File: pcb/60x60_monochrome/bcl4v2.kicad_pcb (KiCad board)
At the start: 2 copper layers, 60 x 60 mm, 56 parts, among them J1 Conn_01x05, J10 Conn_01x01_Female, J11 Conn_01x01_Female, J12 Conn_01x01_Female, J13 Conn_01x01_Female, J14 Conn_01x02, J15 Conn_01x04, J2 Conn_01x05, J3 USB_OTG, J4 Conn_01x05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

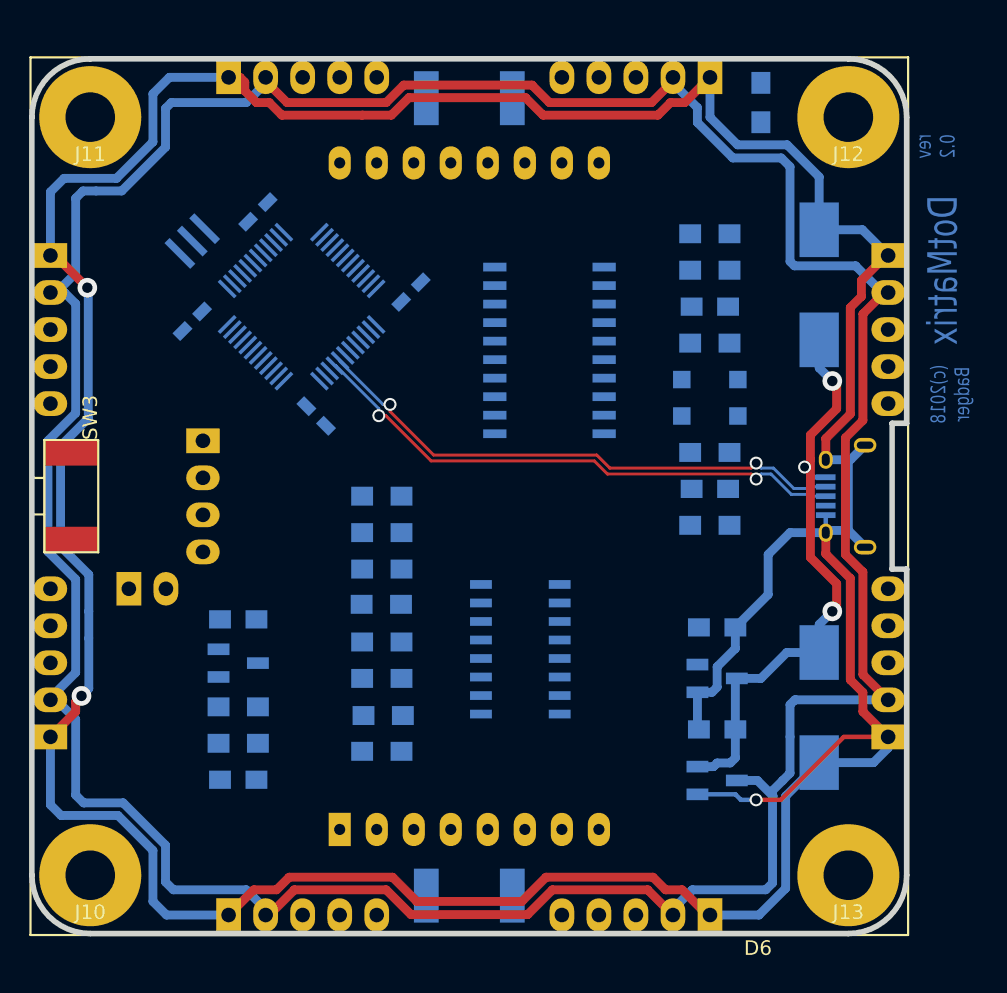
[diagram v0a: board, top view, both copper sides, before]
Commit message: - fix some footprints to reduce ERC errors
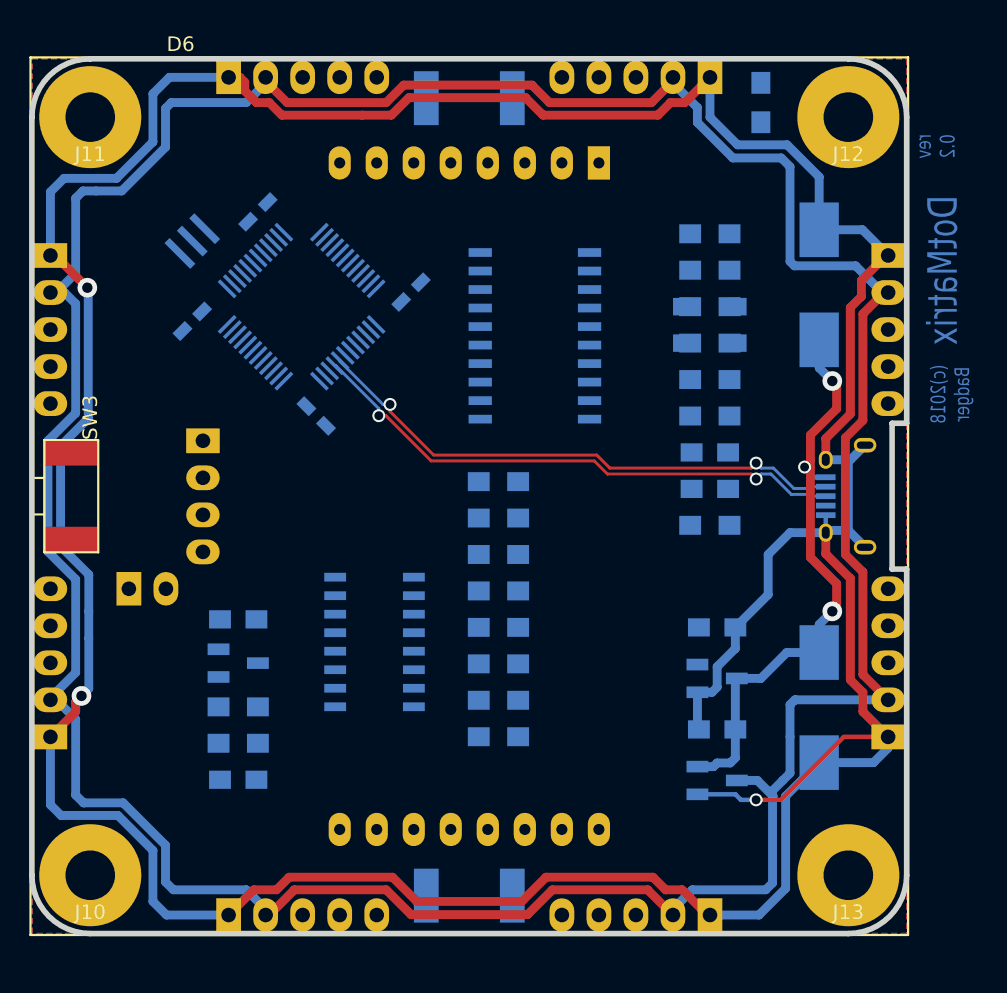
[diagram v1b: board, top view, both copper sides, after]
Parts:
- added R15: R, Resistors_SMD:R_0805_HandSoldering, B.Cu at (116.5, 89.5)
- added R17: R, Resistors_SMD:R_0805_HandSoldering, B.Cu at (116.5, 87.0)
- moved R3 12.0 mm to (102.0, 109.0), turned to 180 degrees
- moved U3 10.0 mm to (93.5, 110.0), turned to 180 degrees
- moved C2 10.0 mm to (116.5, 97.0)
- moved R14 10.0 mm to (116.5, 94.5)
- moved R6 10.0 mm to (102.0, 111.5), turned to 180 degrees
- moved R8 8.94 mm to (102.0, 116.5), turned to 180 degrees
- moved R11 8.73 mm to (102.0, 101.5), turned to 180 degrees
- moved R12 8.73 mm to (102.0, 99.0), turned to 180 degrees
- moved R9 8.73 mm to (102.0, 106.5), turned to 180 degrees
- moved R10 8.73 mm to (102.0, 104.0), turned to 180 degrees
- moved R7 7.97 mm to (102.0, 114.0), turned to 180 degrees
- moved D1 5.00 mm to (116.5, 87.0)
- moved D2 5.00 mm to (116.5, 89.5)
- moved R1 5.00 mm to (116.5, 84.5)
- moved R4 5.00 mm to (116.5, 92.0)
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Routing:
- added copper zone on B.Cu, net GND
- added copper zone on F.Cu, net GND
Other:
- board text added: "or"

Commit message: - imported freeroute output
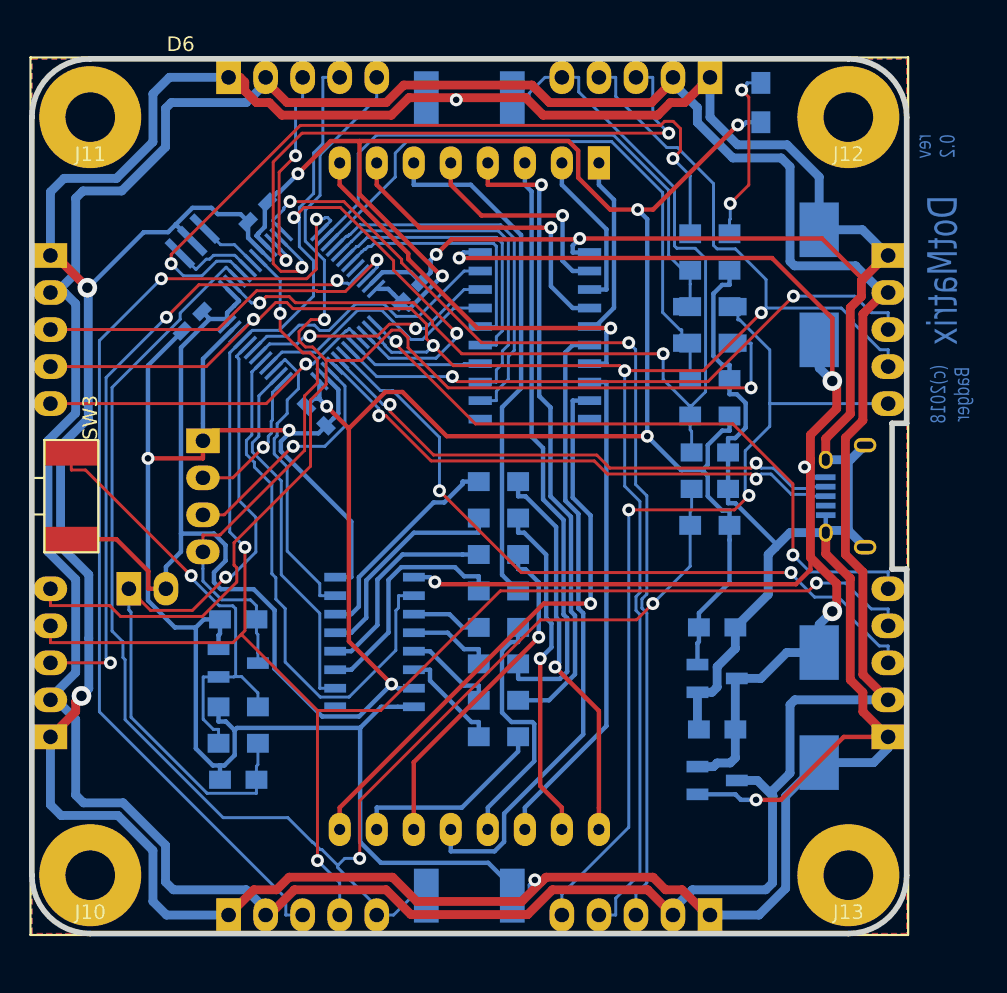
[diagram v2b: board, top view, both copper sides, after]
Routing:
- net +3V3: track 0.00 -> 210.5 mm, vias 0 -> 7
- net GND: track 275.2 -> 479.2 mm, vias 3 -> 9
- net /I2C_SDA: track 0.00 -> 149.2 mm, vias 0 -> 5
- net /I2C_SCL: track 0.00 -> 135.0 mm, vias 0 -> 4
- net /BTN1: track 0.00 -> 103.7 mm, vias 0 -> 2
- net /IN1P: track 0.00 -> 94.1 mm, vias 0 -> 2
- net /BTN0: track 0.00 -> 72.3 mm, vias 0 -> 2
- net /UART_TX2: track 0.00 -> 70.7 mm, vias 0 -> 2
- net /UART_RX2: track 0.00 -> 68.4 mm, vias 0 -> 2
- net +5V: track 42.6 -> 104.5 mm, vias 3 -> 5
- net /IN0P: track 0.00 -> 61.8 mm, vias 0 -> 2
- net /LED: track 0.00 -> 53.5 mm, vias 0 -> 2
- net /BOOT0: track 0.00 -> 49.2 mm, vias 0 -> 1
- net /UART_RX1: track 0.00 -> 49.2 mm, vias 0 -> 2
- net /IN2: track 0.00 -> 46.3 mm, vias 0 -> 2
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
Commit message: - routed pcb, filled zones
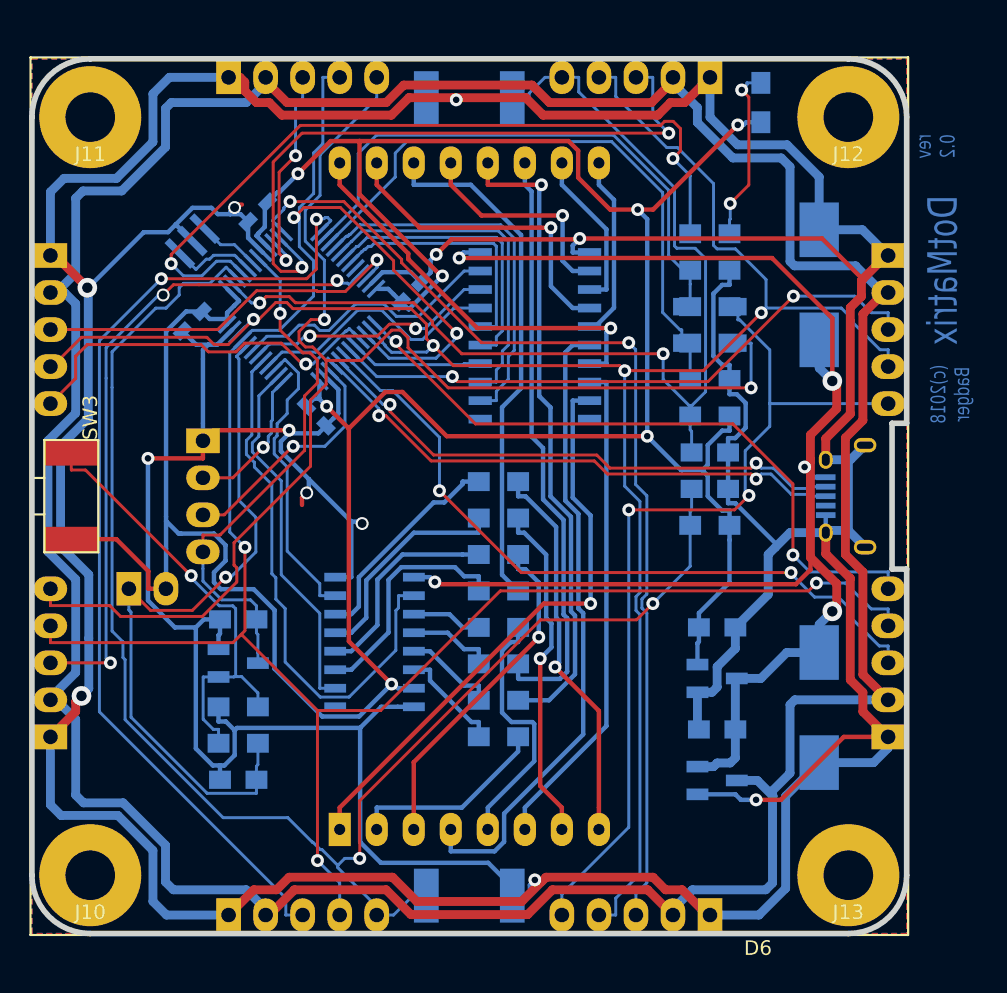
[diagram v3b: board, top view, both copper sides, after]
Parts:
- turned D6 to 0 degrees
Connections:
- J10 pad 1: (no net) -> Net-(J10-Pad1)
- J11 pad 1: (no net) -> Net-(J11-Pad1)
- J12 pad 1: (no net) -> Net-(J12-Pad1)
- J13 pad 1: (no net) -> Net-(J13-Pad1)
- J3 pad 4: (no net) -> Net-(J3-Pad4)
- U2 pad 20: (no net) -> Net-(U2-Pad20)
- U3 pad 9: (no net) -> Net-(U3-Pad9)
- U4 pad 1: (no net) -> Net-(U4-Pad1)
- U4 pad 20: (no net) -> Net-(U4-Pad20)
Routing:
- net /LED_matrix/OUT_A1: track 34.2 -> 54.7 mm, vias 0 -> 1
- net /LED_matrix/OUT_C4: track 13.8 -> 1.01 mm
- net /LED_matrix/OUT_C6: track 23.3 -> 15.6 mm, vias 1 -> 0
- net GND: track 479.2 -> 476.1 mm, vias 9 -> 12
- net /IN3: track 23.7 -> 26.2 mm
- net +3V3: track 210.5 -> 212.9 mm
- net /BTN1: track 103.7 -> 105.1 mm
- net /UART_TX3: track 44.5 -> 45.7 mm
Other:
- board text added: "3V3"
- board text added: "BOOT0"
- board text added: "Btn. debounce"
- board text added: "C6-9 optional, they are for better MCU power stability Y1 optional, e.g. USB needs it"
- board text added: "IN0, IN1 pins voltage shift/div"
- board text added: "Power Supply"
- board text added: "SW3 <1s reset >3s bootloader"
- board text added: "boot selection"

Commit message: - fix silkscreen
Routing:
- net /LED_matrix/OUT_C3: track 44.5 -> 70.9 mm, vias 1 -> 0
- net /LED_matrix/OUT_A3: track 43.6 -> 17.2 mm, vias 0 -> 1
- net /LED_matrix/OUT_A4: track 12.6 -> 34.1 mm
- net /LED_matrix/OUT_A0: track 40.1 -> 18.6 mm
- net /LED_matrix/OUT_C4: track 1.01 -> 22.3 mm
- net /LED_matrix/OUT_C8: track 26.7 -> 12.7 mm, vias 1 -> 0
- net /LED_matrix/OUT_A2: track 28.1 -> 42.1 mm, vias 1 -> 2
- net /LED_matrix/OUT_A1: track 54.7 -> 43.0 mm, vias 1 -> 0
- net /LED_matrix/OUT_C5: track 35.7 -> 26.9 mm
- net /LED_matrix/OUT_A6: track 11.1 -> 2.65 mm
- net /LED_matrix/OUT_C6: track 15.6 -> 21.8 mm
- net /LED_matrix/OUT_C1: track 17.7 -> 15.5 mm, vias 0 -> 1
- net /LED_matrix/OUT_A7: track 15.3 -> 17.5 mm, vias 1 -> 0
- net /LED_matrix/OUT_C2: track 40.7 -> 42.2 mm, vias 0 -> 1
- net /LED_matrix/OUT_C7: track 23.5 -> 24.3 mm
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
